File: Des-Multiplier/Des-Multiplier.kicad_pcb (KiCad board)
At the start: 2 copper layers, 100 x 100 mm, 51 parts, among them SW1 SW_Push, SW2 SW_DIP_x04, SW3 SW_DIP_x04, U1 NE555P, U10 74HC00, U11 74HC00, U12 74LS194, U13 74HC00, U14 74HC00, U2 NE555P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

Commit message: pcb layout draft
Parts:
- added J1: Conn_01x04_Male, Connector_PinHeader_2.54mm:PinHeader_1x04_P2.54mm_Vertical, F.Cu at (103.8, 62.0)
- added J2: Conn_01x04_Male, Connector_PinHeader_2.54mm:PinHeader_1x04_P2.54mm_Vertical, F.Cu at (115.8, 62.0)
- added J3: Conn_01x08_Male, Connector_PinHeader_2.54mm:PinHeader_1x08_P2.54mm_Vertical, F.Cu at (103.8, 56.4)
- added J4: Conn_01x02_Male, Connector_PinHeader_2.54mm:PinHeader_1x02_P2.54mm_Vertical, F.Cu at (129.2, 57.6)
- added J5: R, Resistor_THT:R_Axial_DIN0207_L6.3mm_D2.5mm_P7.62mm_Horizontal, F.Cu at (127.6, 132.4)
- added J6: Conn_01x02_Male, Connector_PinHeader_2.54mm:PinHeader_1x02_P2.54mm_Vertical, F.Cu at (135.0, 57.6)
- moved U8 282.6 mm to (104.2, 107.0)
- moved R17 267.0 mm to (104.8, 70.4), turned to 270 degrees
- moved U7 266.3 mm to (104.1, 130.8)
- moved U12 266.2 mm to (115.6, 130.8)
- moved R14 258.6 mm to (119.6, 70.2), turned to 270 degrees
- moved U4 258.2 mm to (115.6, 106.9)
- moved R16 257.4 mm to (109.8, 70.2), turned to 270 degrees
- moved R15 254.9 mm to (114.8, 70.2), turned to 270 degrees
- moved U5 254.2 mm to (138.6, 121.9), turned to 90 degrees
- moved U3 247.3 mm to (104.2, 83.0)
- moved R12 241.6 mm to (126.6, 123.0)
- moved R13 241.0 mm to (126.6, 127.8)
- moved R11 226.4 mm to (126.6, 118.2)
- moved R20 223.2 mm to (131.2, 150.8), turned to 90 degrees
- moved R10 222.5 mm to (126.6, 113.2)
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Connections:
- net Net-(D1-Pad2) renamed /Out0
- net Net-(D2-Pad2) renamed /Out1
- net Net-(D3-Pad2) renamed /Out2
- net Net-(D4-Pad2) renamed /Out3
- net Net-(D5-Pad2) renamed /Out4
- net Net-(D6-Pad2) renamed /Out5
- net Net-(D7-Pad2) renamed /Out6
- net Net-(D8-Pad2) renamed /Out7
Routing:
- net /~DSP: track 0.00 -> 29.1 mm

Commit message: board changes
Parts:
- removed J4, J6: Conn_01x02_Male, Connector_PinHeader_2.54mm:PinHeader_1x02_P2.54mm_Vertical
- removed SW1: SW_Push, Button_Switch_THT:SW_PUSH_6mm
- added Control: Conn_01x02_Male, Connector_PinHeader_2.54mm:PinHeader_1x02_P2.54mm_Vertical, F.Cu at (129.2, 57.6)
- added Multiply: SW_Push, Button_Switch_THT:SW_PUSH_6mm, F.Cu at (146.5, 105.0)
- added Power: Conn_01x02_Male, Connector_PinHeader_2.54mm:PinHeader_1x02_P2.54mm_Vertical, F.Cu at (135.0, 57.6)
- A Input: renamed from J2
- A Input Switch: renamed from SW3
- B Input: renamed from J1
- B Input Switch: renamed from SW2
- moved A Input 13.2 mm to (102.6, 62.1)
- moved B Input 10.8 mm to (114.6, 62.1)
- renumbered J5 to Jumper, J3 to Output
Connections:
- Jumper pad 1: /~DSP -> /~DSP1
- U6 pad 1: /~DSP -> /~DSP1
- U6 pad 19: /~DSP -> /~DSP1
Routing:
- net GND: track 0.00 -> 471.6 mm
- net +5V: track 0.00 -> 405.1 mm
- net /CLK: track 0.00 -> 217.1 mm
- net /A1: track 0.00 -> 189.2 mm, vias 0 -> 1
- net /~Ashift~\Load: track 0.00 -> 180.9 mm, vias 0 -> 1
- net /A0: track 0.00 -> 176.6 mm, vias 0 -> 1
- net /Out0: track 0.00 -> 166.0 mm
- net /B2: track 0.00 -> 162.5 mm
- net /B3: track 0.00 -> 155.8 mm
- net /A2: track 0.00 -> 153.1 mm
- net /Out2: track 0.00 -> 152.5 mm
- net /B0: track 0.00 -> 152.4 mm
- net /Out1: track 0.00 -> 151.1 mm
- net /B1: track 0.00 -> 150.7 mm
- net /A3: track 0.00 -> 149.5 mm
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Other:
- net class Special added: clearance 0, trace_width 0.25, via_dia 0.8, via_drill 0.4
- rule via_min_size: 0.4 -> 0.2
- board text added: "+5v"
- board text added: "ENSC3020 Multiplier Project 2021 Theo Andily Devika Prasad John Wallis David Wilson"
- board text added: "GND"

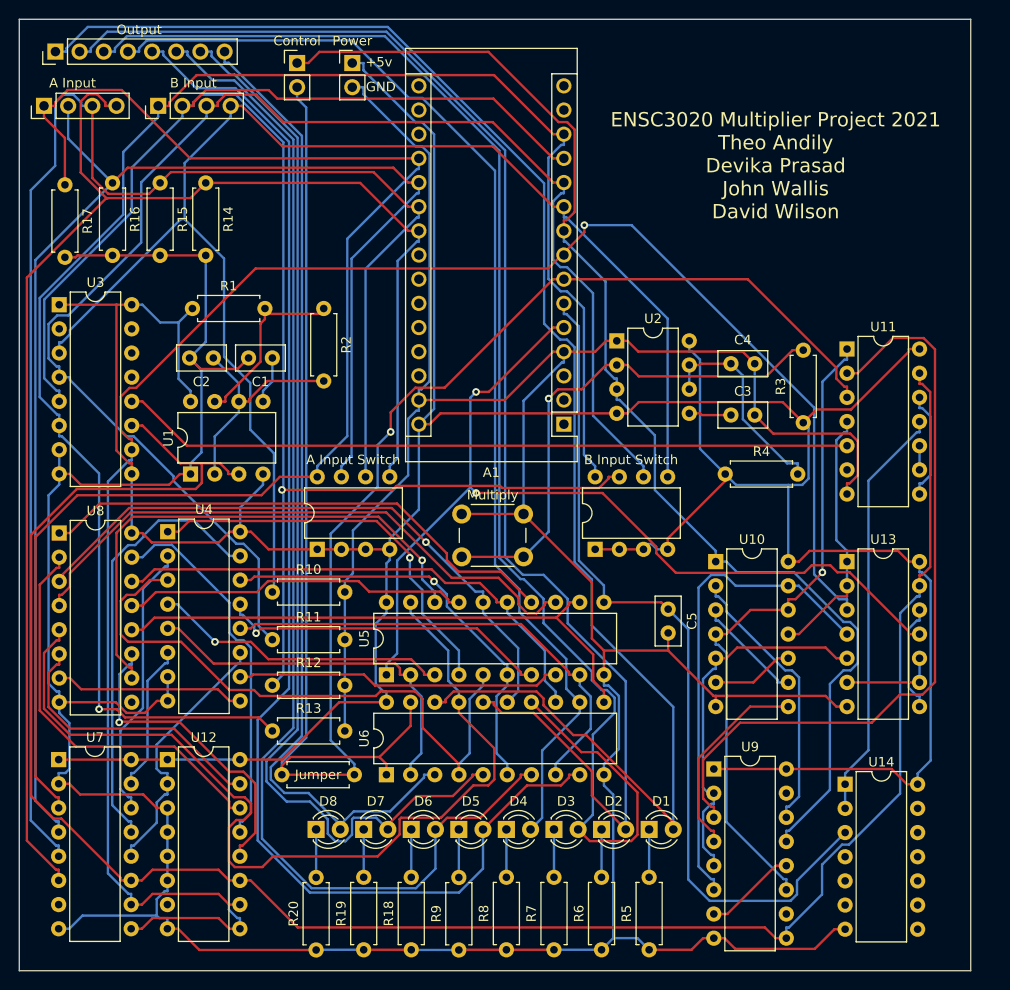
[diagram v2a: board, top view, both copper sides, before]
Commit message: mounting hole respins
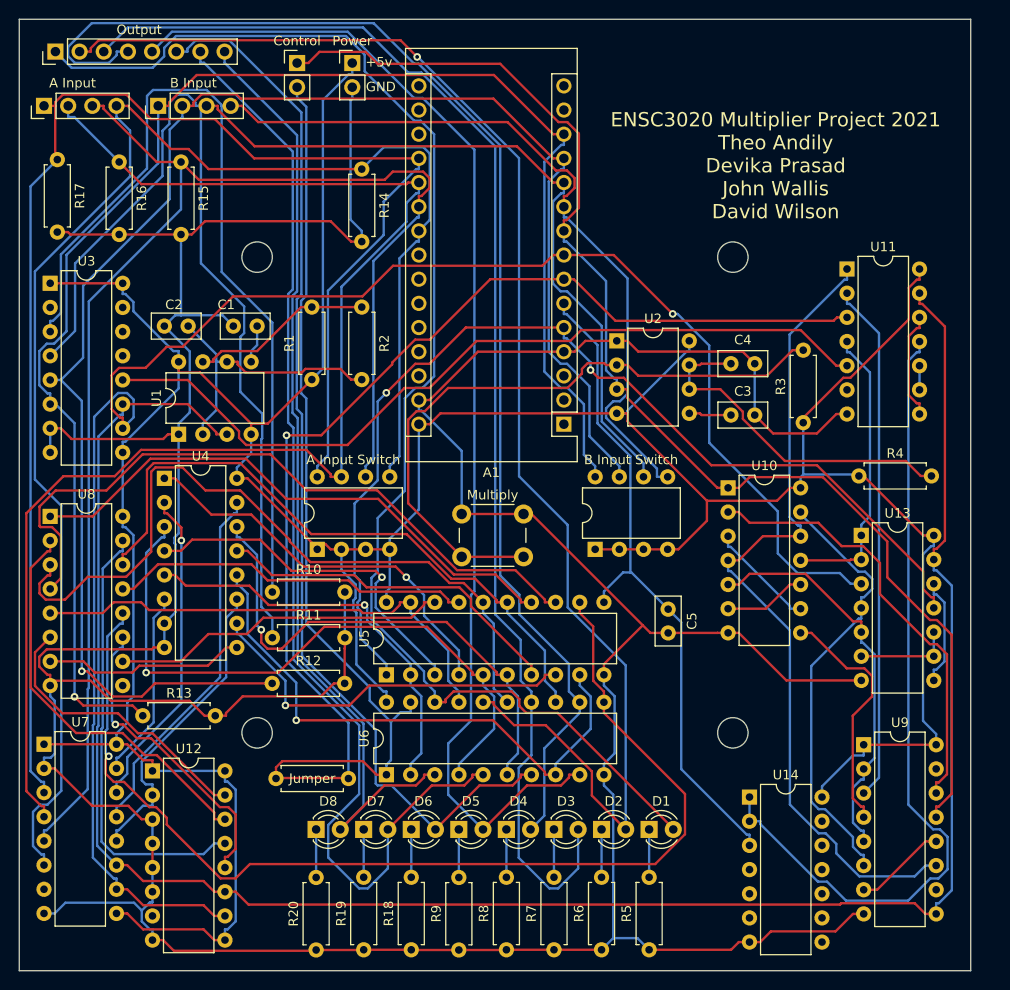
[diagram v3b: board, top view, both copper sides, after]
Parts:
- added REF1: MountingHole_3.2mm_M3, MountingHole:MountingHole_3.2mm_M3, F.Cu at (175.0, 78.0)
- added REF2: MountingHole_3.2mm_M3, MountingHole:MountingHole_3.2mm_M3, F.Cu at (175.0, 128.0)
- added REF3: MountingHole_3.2mm_M3, MountingHole:MountingHole_3.2mm_M3, F.Cu at (125.0, 128.0)
- added REF4: MountingHole_3.2mm_M3, MountingHole:MountingHole_3.2mm_M3, F.Cu at (125.0, 78.0)
- moved R14 16.5 mm to (136.0, 68.8)
- moved U9 16.0 mm to (188.8, 129.2)
- moved R1 14.6 mm to (130.8, 90.9), turned to 90 degrees
- moved R4 14.1 mm to (188.2, 101.0)
- moved R13 13.7 mm to (113.0, 126.2)
- moved U14 10.1 mm to (176.8, 134.8)
- moved U11 8.41 mm to (187.0, 79.2)
- moved U10 7.86 mm to (174.5, 102.2)
- moved U4 5.62 mm to (115.2, 101.2)
- moved U1 4.36 mm to (116.8, 96.6)
- moved C2 4.27 mm to (117.8, 85.2)
- moved R2 4.00 mm to (136.0, 83.2)
- moved C1 3.71 mm to (125.0, 85.2)
- moved U13 3.13 mm to (188.5, 107.2)
- moved R15 3.11 mm to (117.0, 68.0)
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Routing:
- net /Acc4: track 59.4 -> 114.8 mm, vias 0 -> 1
- net /Acc7: track 97.6 -> 52.0 mm
- net /~AccCLK: track 44.1 -> 86.6 mm
- net /~State0: track 80.7 -> 54.8 mm
- net /A3: track 149.5 -> 171.2 mm
- net /AccCLK: track 90.9 -> 70.2 mm
- net /Out0: track 166.0 -> 145.5 mm
- net Net-(U5-Pad18): track 55.8 -> 35.5 mm, vias 1 -> 0
- net /A2: track 153.1 -> 173.2 mm
- net /A1: track 189.2 -> 169.8 mm
- net /~State2: track 69.6 -> 88.1 mm, vias 1 -> 0
- net /Out3: track 120.0 -> 137.5 mm
- net /Out5: track 129.2 -> 112.0 mm
- net /~GoDetect: track 29.3 -> 46.3 mm
- net /Out2: track 152.5 -> 136.8 mm
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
